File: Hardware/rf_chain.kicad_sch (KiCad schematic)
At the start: 10 parts, among them J1 132225, J2 132225, U3 Si4464, U4 Si4464

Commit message: Added oscillators, reset button, and finalized ETH connection
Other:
- company: (none) -> Thomas Montano
- title: (none) -> RF Modems and Front End
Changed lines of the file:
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@@
 	(generator_version "9.0")
 	(paper "A4")
+	(title_block
+		(title "RF Modems and Front End")
+		(date "2025-06-25")
+		(rev "1")
+		(company "Thomas Montano")
+	)
 	(junction
 		(at 69.85 133.35)

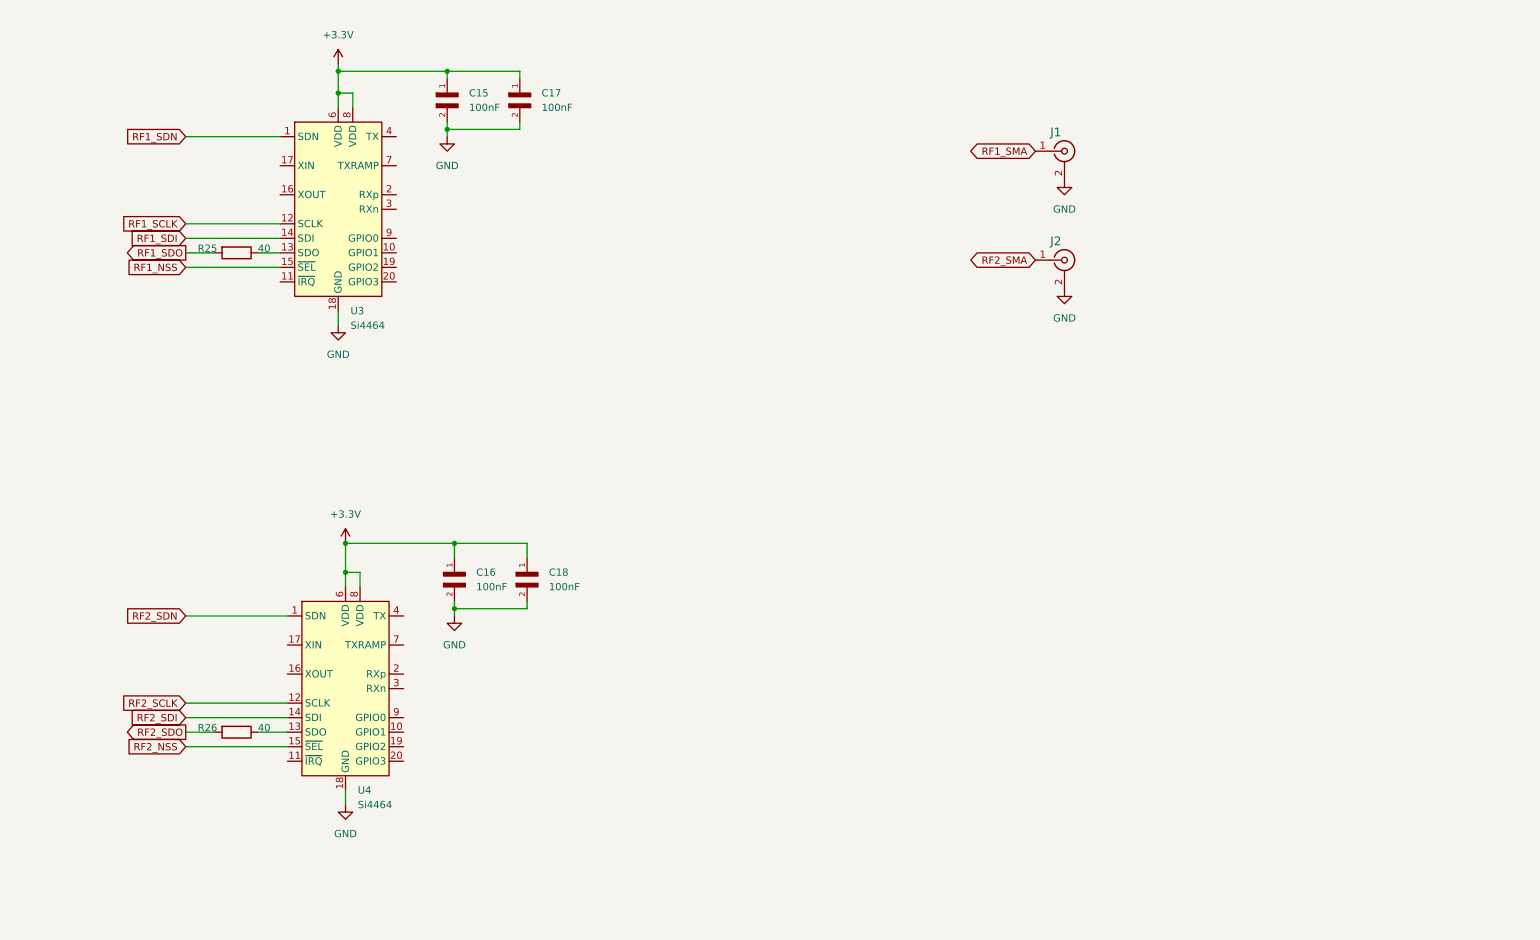
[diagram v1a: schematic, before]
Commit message: changed to SI4468, added 30 MHz oscillators, and connected it to MCU
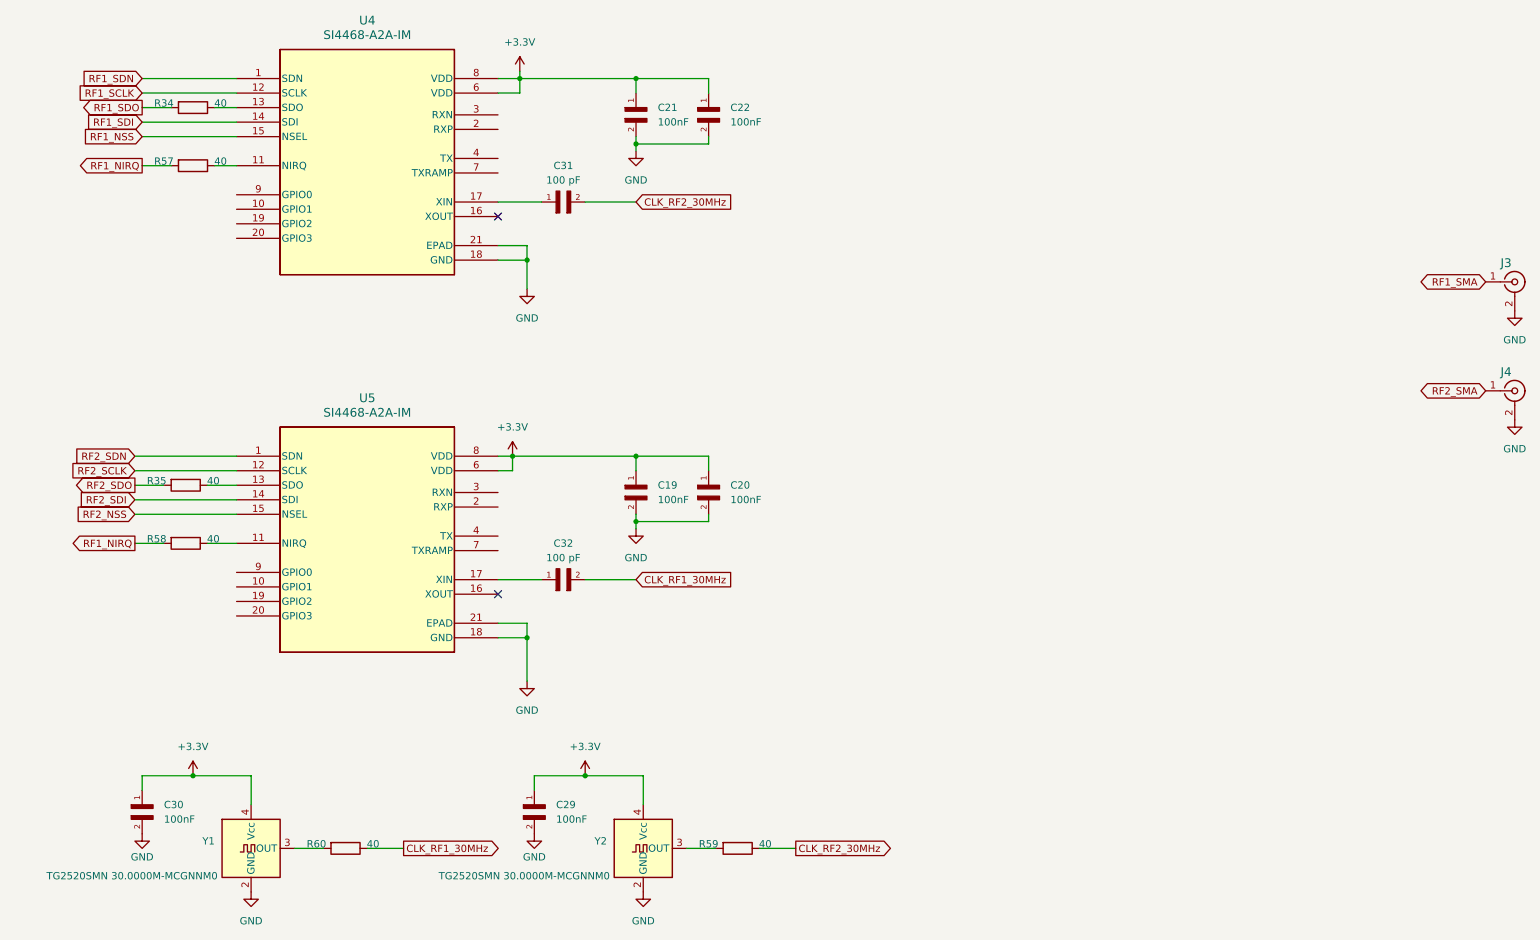
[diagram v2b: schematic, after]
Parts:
- removed U3, U4: Si4464, Package_DFN_QFN:QFN-20-1EP_4x4mm_P0.5mm_EP2.6x2.6mm_ThermalVias, symbol RF:Si4464
- added C29, C30: 100nF, C0402C104J8RACTU:CAPC10555_55N_KEM-L, symbol 2025-06-22_21-59-05:C0402C104J8RACTU
- added C31, C32: 100 pF, 0603ZA101FAT2A:CAPC1608X90N, symbol 0603ZA101FAT2A:0603ZA101FAT2A
- added R57, R58, R59, R60: 40, Resistor_SMD:R_0402_1005Metric, symbol Device:R
- added U4, U5: SI4468-A2A-IM, SI4468_A2A_IM:QFN50P400X400X90-21N, symbol 2025-06-25_20-47-50:SI4468-A2A-IM
- added Y1, Y2: TG2520SMN 30.0000M-MCGNNM0, TG2520SMN:TG2520SMN, symbol TG2520SMN:TG2520SMN 30.0000M-MCGNNM0
- renumbered C16 to C19, C18 to C20, C15 to C21, C17 to C22, J1 to J3, J2 to J4, R25 to R34, R26 to R35
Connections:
- net +3.3V: now also C29.1, C30.1, U4.6 (VDD), U4.8 (VDD), U5.6 (VDD), U5.8 (VDD), Y1.4 (Vcc), Y2.4 (Vcc)
- net GND: now also C29.2, C30.2, U4.18 (GND), U4.21 (EPAD), U5.18 (GND), U5.21 (EPAD), Y1.2 (GND), Y2.2 (GND)
- net RF1_NSS: now also U4.15 (NSEL)
- net RF1_SCLK: now also U4.12 (SCLK)
- net RF1_SDI: now also U4.14 (SDI)
- net RF1_SDN: now also U4.1 (SDN)
- net RF2_NSS: now also U5.15 (NSEL)
- net RF2_SCLK: now also U5.12 (SCLK)
- net RF2_SDI: now also U5.14 (SDI)
- net RF2_SDN: now also U5.1 (SDN)
- net at R34.1: now also U4.13 (SDO)
- net at R35.1: now also U5.13 (SDO)
- new net: R58.1, U5.11 (NIRQ)
- new net: C32.1, U5.17 (XIN)
- new net: R60.2, Y1.3 (OUT)
- new net: C31.1, U4.17 (XIN)
- new net: R59.2, Y2.3 (OUT)
- new net: R57.1, U4.11 (NIRQ)
- new net CLK_RF1_30MHz: C32.2, R60.1
- new net CLK_RF2_30MHz: C31.2, R59.1
- new net RF1_NIRQ: R57.2, R58.2
- no-connect marks 0 -> 2
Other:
- moved on the sheet: C19, C20, C21, C22, J3, J4, R34, R35

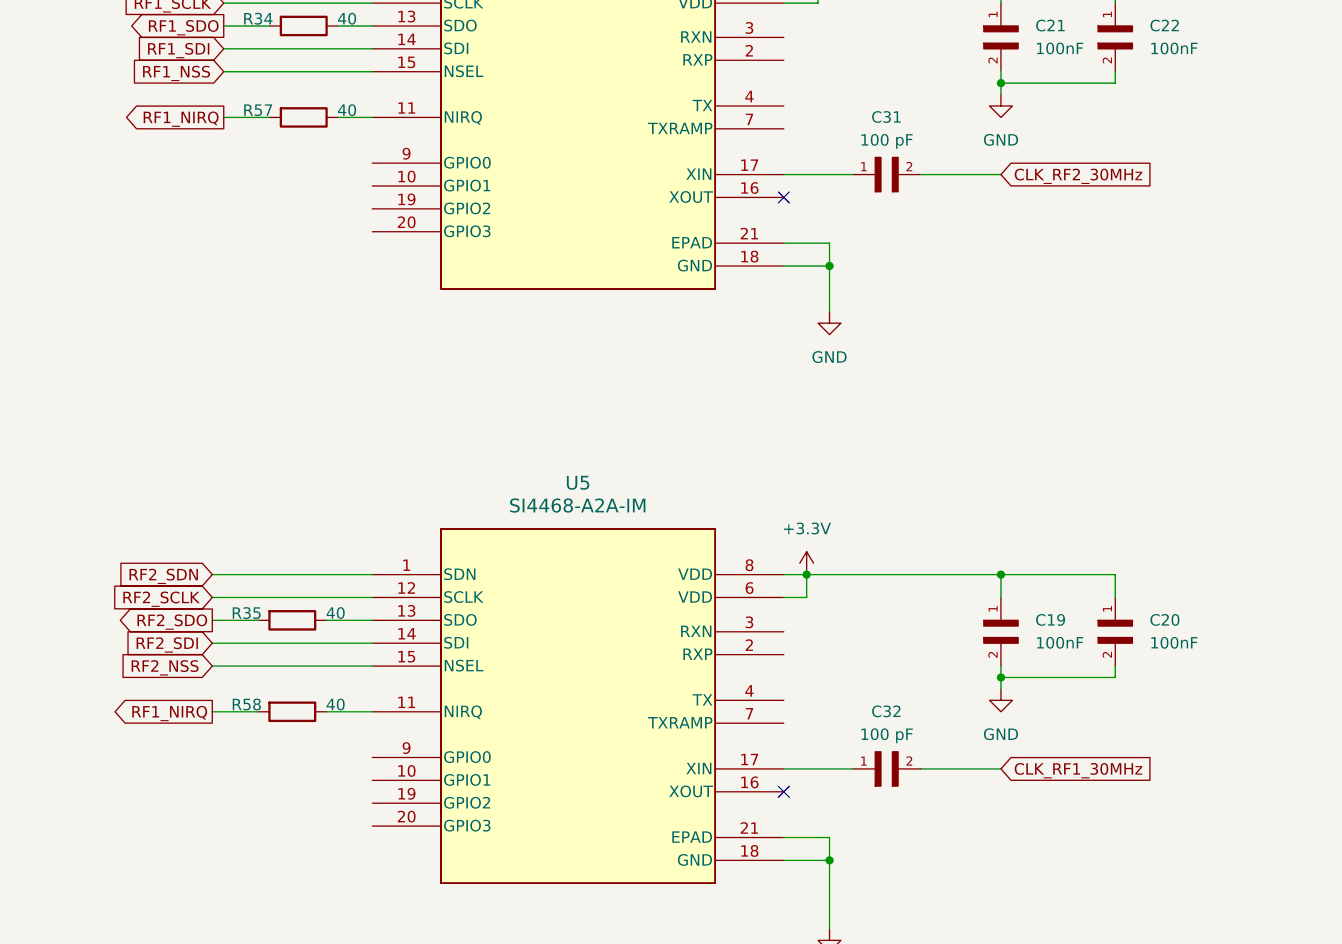
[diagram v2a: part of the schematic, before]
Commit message: fixed incorrect naming on RF clk and connected RF NIRQ lines
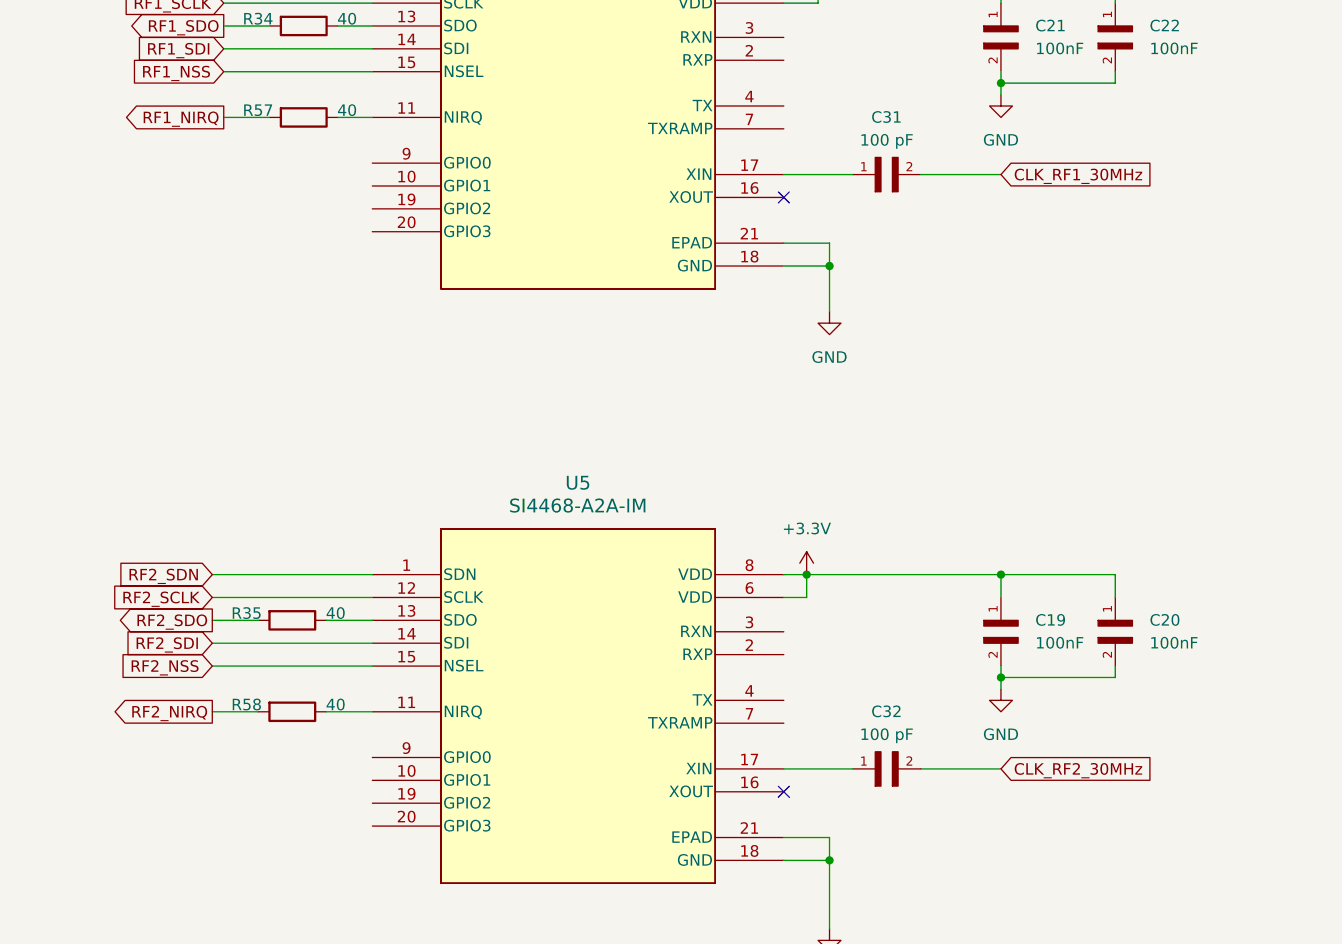
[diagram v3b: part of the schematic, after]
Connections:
- net CLK_RF1_30MHz: now also C31.2; no longer C32.2
- net CLK_RF2_30MHz: now also C32.2; no longer C31.2
- net RF1_NIRQ: no longer R58.2
- new net RF2_NIRQ: R58.2
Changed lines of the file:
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@@
 		)
 	)
-	(global_label "CLK_RF1_30MHz"
+	(global_label "CLK_RF2_30MHz"
 		(shape input)
 		(at 120.65 134.62 0)
@@
 		)
 	)
-	(global_label "RF1_NIRQ"
+	(global_label "RF2_NIRQ"
 		(shape output)
 		(at 33.02 128.27 180)
@@
 		)
 	)
-	(global_label "CLK_RF2_30MHz"
+	(global_label "CLK_RF1_30MHz"
 		(shape input)
 		(at 120.65 68.58 0)
